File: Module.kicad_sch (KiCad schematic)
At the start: 10 parts, among them J2 HOLDDOWN, U2 74AUP1G07, U8 TPS259520DSGR

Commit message: all parts geo-renamed
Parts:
- renumbered C37 to 1C13, C23 to 1C14, J2 to 1J1, J1 to 1J2, R46 to 1R7, TP1 to 1TP1, U2 to 1U3, U8 to 1U5, C36 to 2C38, R43 to 2R38
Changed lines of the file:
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@@
 		(dnp no)
 		(fields_autoplaced yes)
-		(property "Reference" "U2"
+		(property "Reference" "1U3"
 			(at 78.74 46.9198 0)
 			(effects
@@
 			(project ""
 				(path "/4c939de5-59ef-438d-9f29-5de1016e5f2f"
-					(reference "U2")
+					(reference "1U3")
 					(unit 1)
 				)
@@
 		(on_board yes)
 		(dnp no)
-		(property "Reference" "TP1"
+		(property "Reference" "1TP1"
 			(at 178.816 41.148 0)
 			(effects
@@
 			(project ""
 				(path "/4c939de5-59ef-438d-9f29-5de1016e5f2f"
-					(reference "TP1")
+					(reference "1TP1")
 					(unit 1)
 				)
@@
 		(dnp no)
 		(fields_autoplaced yes)
-		(property "Reference" "U8"
+		(property "Reference" "1U5"
 			(at 156.21 30.48 0)
 			(effects
@@
 			(project ""
 				(path "/4c939de5-59ef-438d-9f29-5de1016e5f2f"
-					(reference "U8")
+					(reference "1U5")
 					(unit 1)
 				)
@@
 		(on_board yes)
 		(dnp no)
-		(property "Reference" "J2"
+		(property "Reference" "1J1"
 			(at 250.19 116.8399 0)
 			(effects
@@
 			(project ""
 				(path "/4c939de5-59ef-438d-9f29-5de1016e5f2f"
-					(reference "J2")
+					(reference "1J1")
 					(unit 1)
 				)
@@
 		(dnp yes)
 		(fields_autoplaced yes)
-		(property "Reference" "C36"
+		(property "Reference" "2C38"
 			(at 138.43 54.6099 0)
 			(effects
@@
 			(project ""
 				(path "/4c939de5-59ef-438d-9f29-5de1016e5f2f"
-					(reference "C36")
+					(reference "2C38")
 					(unit 1)
 				)
@@
 		(dnp no)
 		(fields_autoplaced yes)
-		(property "Reference" "C37"
+		(property "Reference" "1C13"
 			(at 194.31 43.1799 0)
 			(effects
@@
 			(project "ESP32PoE"
 				(path "/4c939de5-59ef-438d-9f29-5de1016e5f2f"
-					(reference "C37")
+					(reference "1C13")
 					(unit 1)
 				)
@@
 		(dnp no)
 		(fields_autoplaced yes)
-		(property "Reference" "R43"
+		(property "Reference" "2R38"
 			(at 50.8 44.4499 0)
 			(effects
@@
 			(project "ESP32PoE"
 				(path "/4c939de5-59ef-438d-9f29-5de1016e5f2f"
-					(reference "R43")
+					(reference "2R38")
 					(unit 1)
 				)
@@
 		(dnp no)
 		(fields_autoplaced yes)
-		(property "Reference" "R46"
+		(property "Reference" "1R7"
 			(at 182.88 53.3399 0)
 			(effects
@@
 			(project "ESP32PoE"
 				(path "/4c939de5-59ef-438d-9f29-5de1016e5f2f"
-					(reference "R46")
+					(reference "1R7")
 					(unit 1)
 				)
@@
 		(dnp no)
 		(fields_autoplaced yes)
-		(property "Reference" "C23"
+		(property "Reference" "1C14"
 			(at 124.46 54.6099 0)
 			(effects
@@
 			(project "ESP32PoE"
 				(path "/4c939de5-59ef-438d-9f29-5de1016e5f2f"
-					(reference "C23")
+					(reference "1C14")
 					(unit 1)
 				)
@@
 		(dnp no)
 		(fields_autoplaced yes)
-		(property "Reference" "J1"
+		(property "Reference" "1J2"
 			(at 243.84 31.75 0)
 			(effects
@@
 			(project ""
 				(path "/4c939de5-59ef-438d-9f29-5de1016e5f2f"
-					(reference "J1")
+					(reference "1J2")
 					(unit 1)
 				)

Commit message: properties cleanup added unique parts ID
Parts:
- 1C13: IDAnything (none) -> 9rwxvasa5ehn0bvjk789fvwtcg
- 1C14: IDAnything (none) -> 5cec8xb21wkrn9jazn0tx4yt0k
- 1R7: IDAnything (none) -> 26egdzngepjd69cx08s4ysz9m1
- 1U3: IDAnything (none) -> 4kejh15d7phrdbc2yeb9rvqcz2
- 1U5: IDAnything (none) -> dx1kt19hzmhzyb3wqtjdqqz0xz
- 2R38: IDAnything (none) -> c1vc3q1ecwg38aepd291cy2avj

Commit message: added test points for PoE stage
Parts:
- 1TP1: footprint TestPoint:TestPoint_Pad_D1.5mm -> TestPoint:TestPoint_Pad_D1.0mm
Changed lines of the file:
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@@
 			)
 		)
-		(property "Footprint" "TestPoint:TestPoint_Pad_D1.5mm"
+		(property "Footprint" "TestPoint:TestPoint_Pad_D1.0mm"
 			(at 185.42 46.99 0)
 			(effects

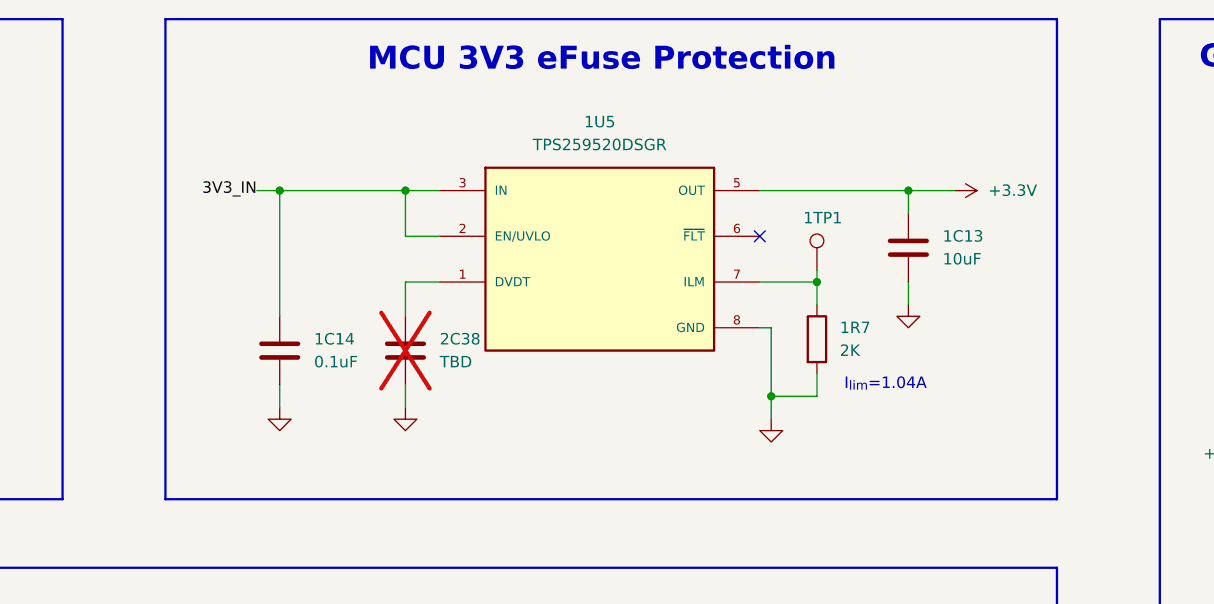
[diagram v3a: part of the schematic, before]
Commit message: ESP32 silk screen enhancement added missing part numbers finalized r0.3 work optimized Ethernet ESD diode position added second 22uF bulk updated transformer footprint courtyard enlarged supply current testpad tented bottom testpad vias for flash/ram increased bulk capacitance after efuse reverted solder paste reduction repositioning and cleanup, footprint reworks
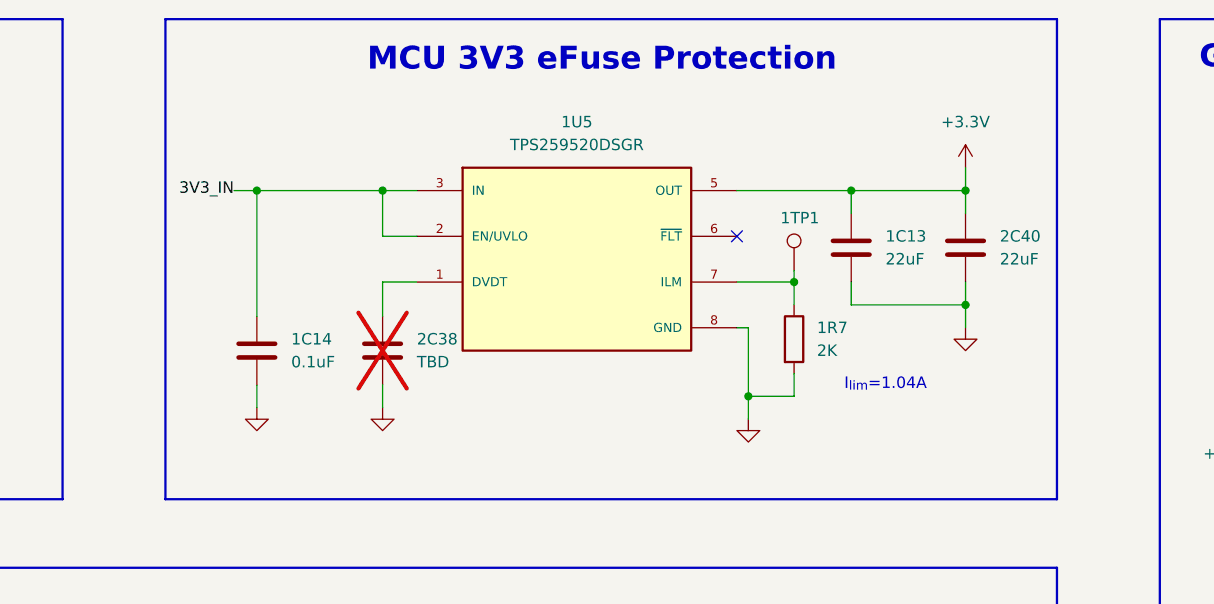
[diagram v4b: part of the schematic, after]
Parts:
- added 2C40: 22uF, Capacitor_SMD:C_0805_2012Metric, symbol Device:C
- 1C13: value 10uF -> 22uF; IDAnything 9rwxvasa5ehn0bvjk789fvwtcg -> 9ywanckr2wg1n8wwt4e0swy1cx; MOUSER# 81-GRM21BR71A106MA3L -> 81-GRM21BZ71A226ME5L
- 1TP1: footprint TestPoint:TestPoint_Pad_D1.0mm -> TestPoint:TestPoint_Pad_D2.0mm
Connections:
- net +3.3V: now also 2C40.1
- net GND: now also 2C40.2
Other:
- moved on the sheet: 1C13, 1C14, 1R7, 1TP1, 1U5, 2C38

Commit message: added some LCSC part numbers
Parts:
- 1U3: LCSC# (none) -> C2675670
- 1U5: LCSC# (none) -> C2860878
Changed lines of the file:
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@@
+			)
+		)
+		(property "LCSC#" "C2675670"
+			(at 66.04 53.34 0)
+			(effects
+				(font
+					(size 1.27 1.27)
+				)
+				(hide yes)
 			)
 		)
@@
 			)
 		)
+		(property "LCSC#" ""
+			(at 177.8 46.99 0)
+			(effects
+				(font
+					(size 1.27 1.27)
+				)
+				(hide yes)
+			)
+		)
 		(pin "1"
 		)
@@
 			)
 		)
+		(property "LCSC#" "C2860878"
+			(at 153.67 45.72 0)
+			(effects
+				(font
+					(size 1.27 1.27)
+				)
+				(hide yes)
+			)
+		)
 		(pin "4"
 		)
@@
 			)
 		)
+		(property "LCSC#" ""
+			(at 248.92 115.57 0)
+			(effects
+				(font
+					(size 1.27 1.27)
+				)
+				(hide yes)
+			)
+		)
 		(pin "2"
 		)
@@
 			)
 		)
+		(property "LCSC#" ""
+			(at 132.08 55.88 0)
+			(effects
+				(font
+					(size 1.27 1.27)
+				)
+				(hide yes)
+			)
+		)
 		(pin "1"
 		)
@@
 			)
 		)
+		(property "LCSC#" ""
+			(at 184.15 44.45 0)
+			(effects
+				(font
+					(size 1.27 1.27)
+				)
+				(hide yes)
+			)
+		)
 		(pin "2"
 		)
@@
 			)
 		)
+		(property "LCSC#" ""
+			(at 196.85 44.45 0)
+			(effects
+				(font
+					(size 1.27 1.27)
+				)
+				(hide yes)
+			)
+		)
 		(pin "2"
 		)
@@
 			)
 		)
+		(property "LCSC#" ""
+			(at 48.26 45.72 0)
+			(effects
+				(font
+					(size 1.27 1.27)
+				)
+				(hide yes)
+			)
+		)
 		(pin "1"
 		)
@@
 			)
 		)
+		(property "LCSC#" ""
+			(at 177.8 54.61 0)
+			(effects
+				(font
+					(size 1.27 1.27)
+				)
+				(hide yes)
+			)
+		)
 		(pin "1"
 		)
@@
 			)
 		)
+		(property "LCSC#" ""
+			(at 118.11 55.88 0)
+			(effects
+				(font
+					(size 1.27 1.27)
+				)
+				(hide yes)
+			)
+		)
 		(pin "1"
 		)
@@
 			(at 243.84 60.96 0)
 			(effects
+				(font
+					(size 1.27 1.27)
+				)
+				(hide yes)
+			)
+		)
+		(property "LCSC#" ""
+			(at 243.84 60.96 0)
+			(effects
